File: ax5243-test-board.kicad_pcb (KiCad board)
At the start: 2 copper layers, 43.2 x 18 mm, 39 parts, among them J1 CONSMA008-G, J2 Conn_01x15, J3 Conn_01x15, U1 AX5243, X1 26MHz

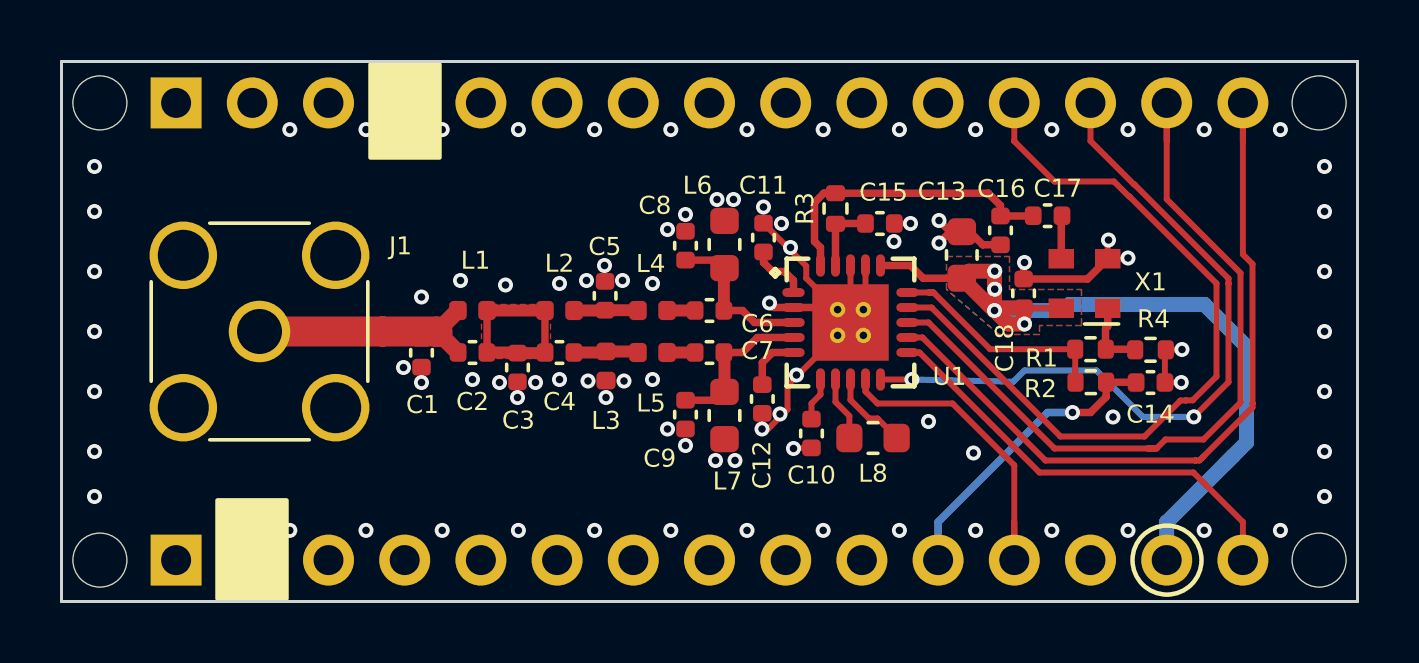
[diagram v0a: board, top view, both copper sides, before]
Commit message: Add additional matching capacitor needed for higher frequencies
This closes: #3
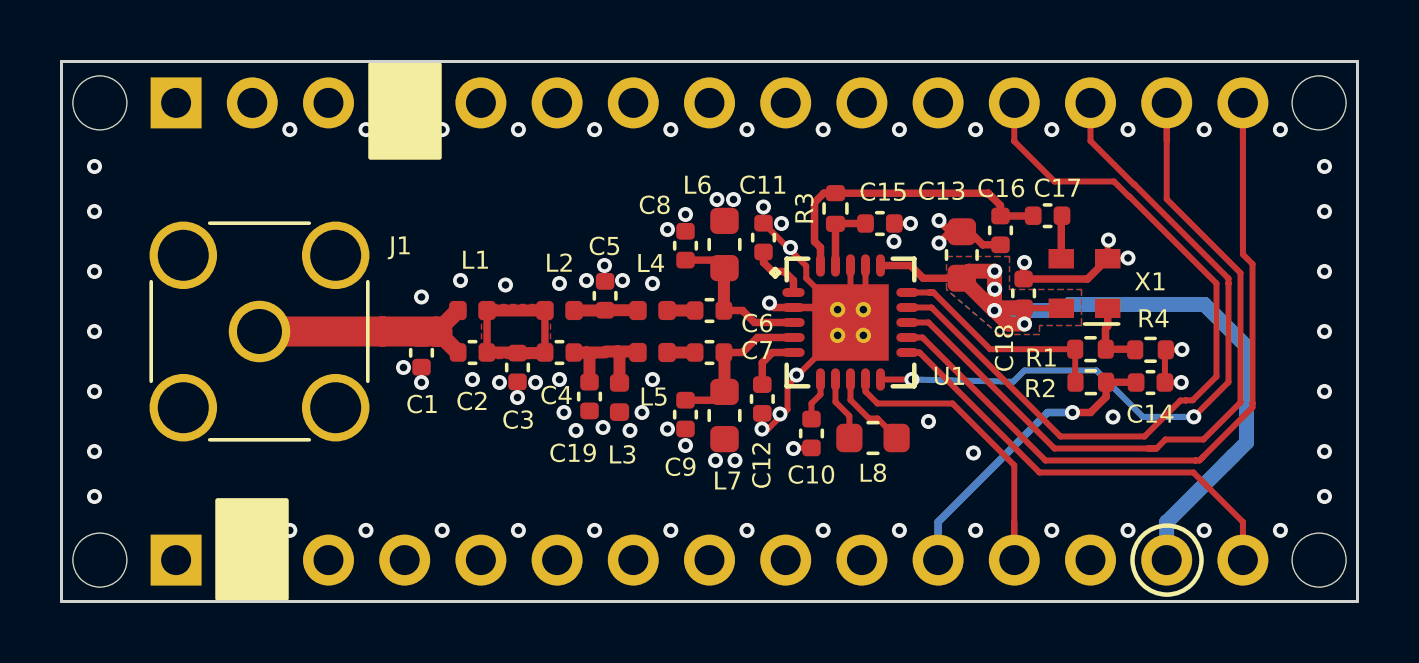
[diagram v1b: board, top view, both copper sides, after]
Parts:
- added C19: DNP, Capacitor_SMD:C_0402_1005Metric, F.Cu at (140.0, 84.2)
- moved L3 1.14 mm to (141.0, 84.2)
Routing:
- net /RF2N: track 2.16 -> 4.27 mm
- net GND: vias 89 -> 91
